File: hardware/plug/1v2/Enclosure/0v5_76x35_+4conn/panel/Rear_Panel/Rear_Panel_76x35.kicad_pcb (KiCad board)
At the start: 2 copper layers, 76 x 35 mm, 6 parts

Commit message: qfix
- #9 documents
- USB and PWR cutout displacement for 0.15 mm
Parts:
- moved REF** 0.15 mm to (56.8, 120.5)
- moved REF** 0.15 mm to (70.6, 120.5)
- moved REF** 0.15 mm to (55.9, 117.8)
- moved REF** 0.15 mm to (71.3, 117.8)
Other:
- outline, holes or cut-outs redrawn

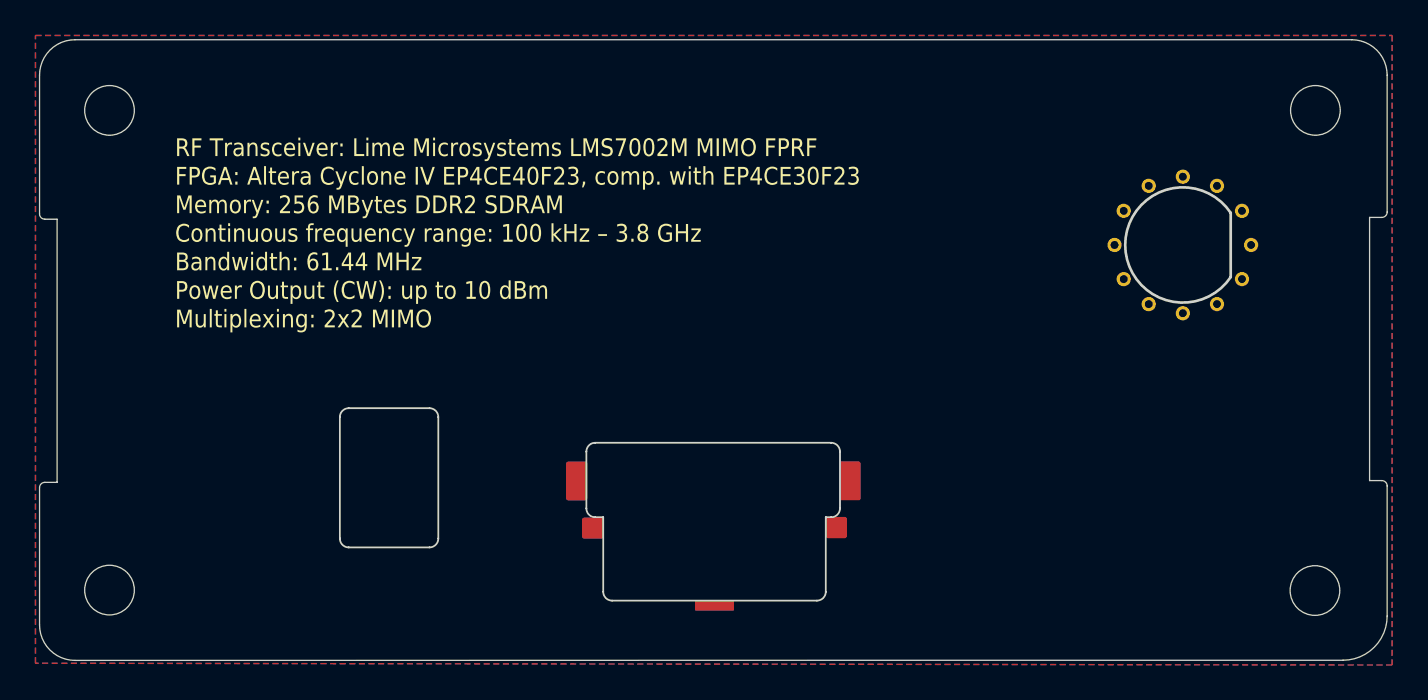
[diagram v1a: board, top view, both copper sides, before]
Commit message: 3rd batch ready for fab house
Gerber output produced
Combined into a panel

Added small holes on backside for "ventilation" #7
Naming is consistent with current LimeSDR boards W, L, H order for TX #2

Text stays on Silkscreen for now #8
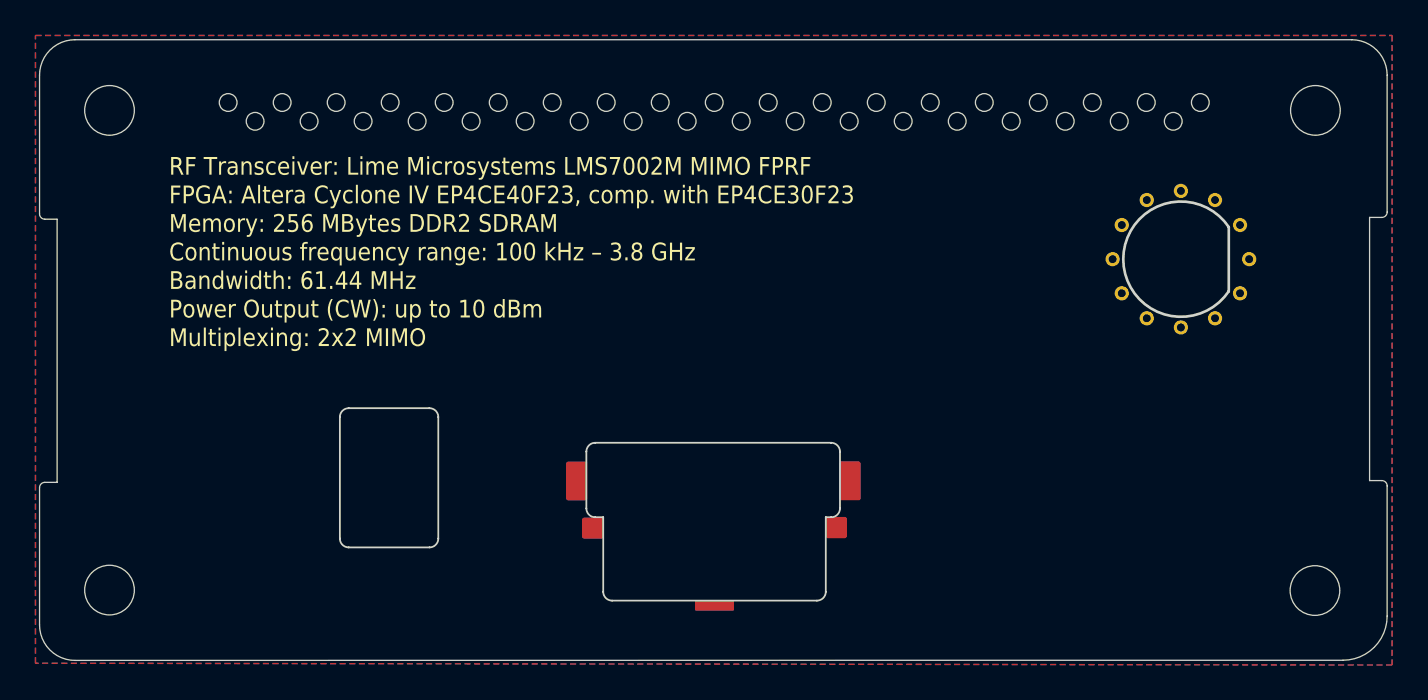
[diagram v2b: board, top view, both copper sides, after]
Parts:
- added REF**: Hole, Ohisja:hole, F.Cu at (43.9, 97.5)
- added REF**: Hole, Ohisja:hole, F.Cu at (68.2, 97.5)
- added REF**: Hole, Ohisja:hole, F.Cu at (71.3, 97.5)
- added REF**: Hole, Ohisja:hole, F.Cu at (65.2, 97.5)
- added REF**: Hole, Ohisja:hole, F.Cu at (56.1, 97.5)
- added REF**: Hole, Ohisja:hole, F.Cu at (89.6, 97.5)
- added REF**: Hole, Ohisja:hole, F.Cu at (80.4, 97.5)
- added REF**: Hole, Ohisja:hole, F.Cu at (83.5, 97.5)
- added REF**: Hole, Ohisja:hole, F.Cu at (86.5, 97.5)
- added REF**: Hole, Ohisja:hole, F.Cu at (77.4, 97.5)
- added REF**: Hole, Ohisja:hole, F.Cu at (91.1, 96.5)
- added REF**: Hole, Ohisja:hole, F.Cu at (46.9, 97.5)
- added REF**: Hole, Ohisja:hole, F.Cu at (88.0, 96.5)
- added REF**: Hole, Ohisja:hole, F.Cu at (85.0, 96.5)
- added REF**: Hole, Ohisja:hole, F.Cu at (81.9, 96.5)
- added REF**: Hole, Ohisja:hole, F.Cu at (78.9, 96.5)
- added REF**: Hole, Ohisja:hole, F.Cu at (75.9, 96.5)
- added REF**: Hole, Ohisja:hole, F.Cu at (72.8, 96.5)
- added REF**: Hole, Ohisja:hole, F.Cu at (69.8, 96.5)
- added REF**: Hole, Ohisja:hole, F.Cu at (66.7, 96.5)
- added REF**: Hole, Ohisja:hole, F.Cu at (63.7, 96.5)
- added REF**: Hole, Ohisja:hole, F.Cu at (60.6, 96.5)
- added REF**: Hole, Ohisja:hole, F.Cu at (37.8, 97.5)
- added REF**: Hole, Ohisja:hole, F.Cu at (57.6, 96.5)
- added REF**: Hole, Ohisja:hole, F.Cu at (54.5, 96.5)
- added REF**: Hole, Ohisja:hole, F.Cu at (51.5, 96.5)
- added REF**: Hole, Ohisja:hole, F.Cu at (48.4, 96.5)
- added REF**: Hole, Ohisja:hole, F.Cu at (45.4, 96.5)
- added REF**: Hole, Ohisja:hole, F.Cu at (42.4, 96.5)
- added REF**: Hole, Ohisja:hole, F.Cu at (39.3, 96.5)
- added REF**: Hole, Ohisja:hole, F.Cu at (53.0, 97.5)
- added REF**: Hole, Ohisja:hole, F.Cu at (40.8, 97.5)
- added REF**: Hole, Ohisja:hole, F.Cu at (50.0, 97.5)
- added REF**: Hole, Ohisja:hole, F.Cu at (74.3, 97.5)
- added REF**: Hole, Ohisja:hole, F.Cu at (59.1, 97.5)
- added REF**: Hole, Ohisja:hole, F.Cu at (62.1, 97.5)
- added REF1: Hole, Ohisja:hole, F.Cu at (36.3, 96.5)
- moved REF** 0.81 mm to (90.0, 105.3)
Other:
- board text added: "20160924"
- board text removed: "20160910"

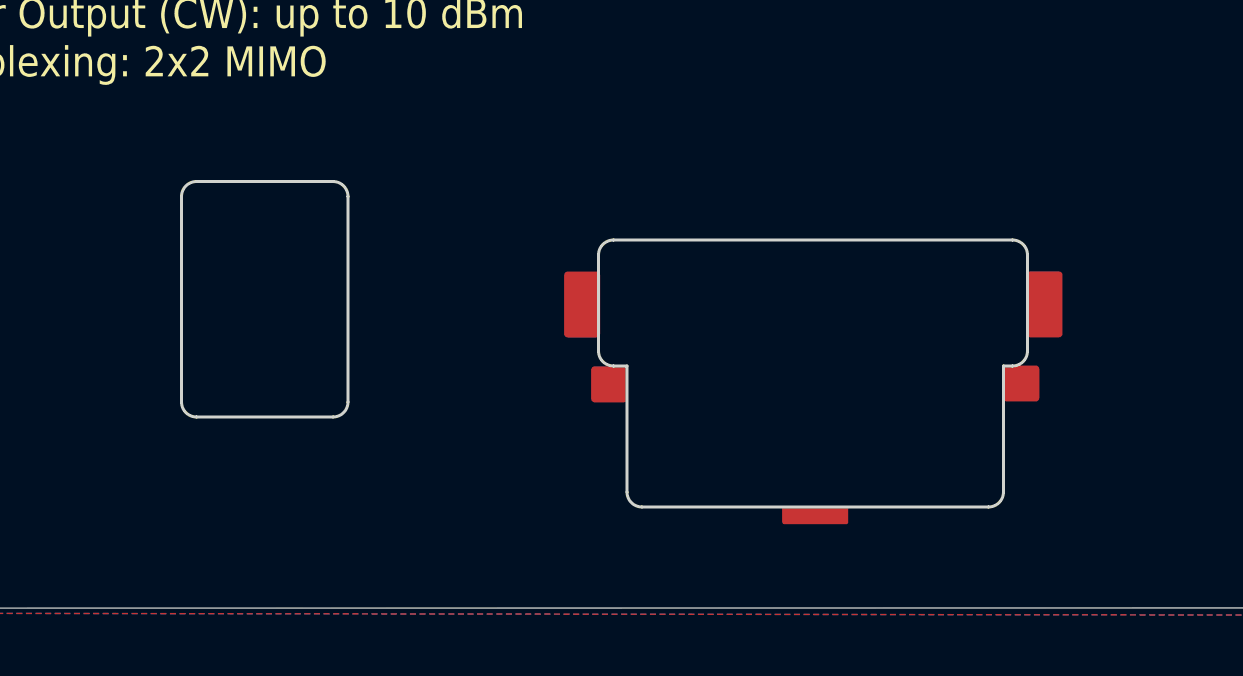
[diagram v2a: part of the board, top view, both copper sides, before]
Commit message: add 3d models in .wrl
used @2ftg .step models and imported them into FreeCAD
added .wrl for Rear panels and hole plugs
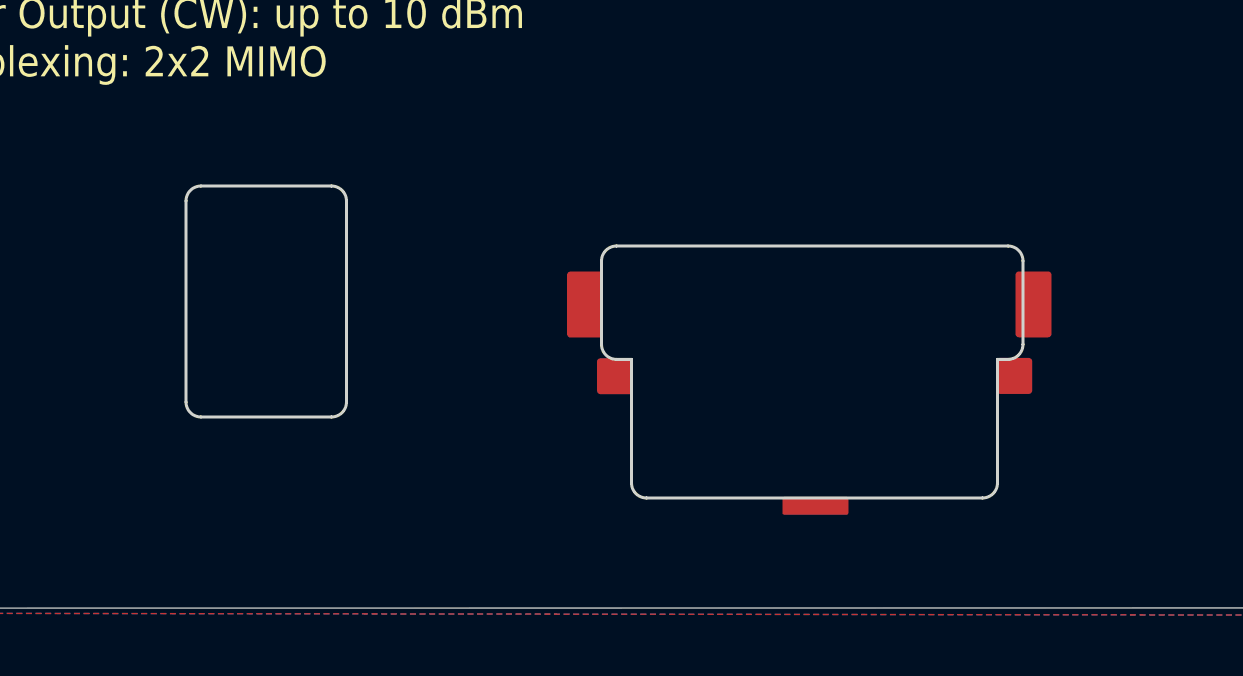
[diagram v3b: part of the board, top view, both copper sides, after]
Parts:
- moved REF** 0.37 mm to (71.0, 117.8)
- moved REF** 0.34 mm to (70.3, 120.2)
- moved REF** 0.33 mm to (57.0, 120.2)
- moved REF** 0.31 mm to (63.7, 124.5)
- moved REF** 0.10 mm to (56.0, 117.8)
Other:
- outline, holes or cut-outs redrawn
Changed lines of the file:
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@@
     (links 16)
     (no_connects 0)
-    (area 25.34 92.7 101.900001 128.200001)
+    (area 25.619999 92.929999 101.630001 127.950001)
     (thickness 1.6)
     (drawings 295)
@@
     (pad_to_mask_clearance 0)
     (aux_axis_origin 24.95 92.3)
-    (grid_origin 24.95 92.3)
+    (grid_origin 56.965227 115.867916)
     (visible_elements 7FFFFFFF)
     (pcbplotparams
@@
   )
   (module Connect:1pin (layer F.Cu)
-    (at 56.82 120.48)
+    (at 57.015227 120.207916)
     (descr "module 1 pin (ou trou mecanique de percage)")
     (tags DEV)
@@
   )
   (module Connect:1pin (layer F.Cu)
-    (at 70.56 120.45)
+    (at 70.325227 120.197916)
     (descr "module 1 pin (ou trou mecanique de percage)")
     (tags DEV)
@@
   )
   (module Connect:1pin (layer F.Cu)
-    (at 63.69 124.84 270)
+    (at 63.695227 124.527916 270)
     (descr "module 1 pin (ou trou mecanique de percage)")
     (tags DEV)
@@
   )
   (module Connect:1pin (layer F.Cu)
-    (at 55.92 117.82 180)
+    (at 56.015227 117.82 180)
     (descr "module 1 pin (ou trou mecanique de percage)")
     (tags DEV)
@@
     (fp_circle (center 0 0) (end 3.83 0) (layer F.Mask) (width 1.35))
     (fp_circle (center 0 0) (end 2.66 0) (layer F.Mask) (width 3))
+    (pad 1 thru_hole circle (at 3.85 0 270) (size 0.8 0.8) (drill 0.45) (layers *.Cu)
+      (net 1 GND))
+    (pad 1 thru_hole circle (at 3.334198 1.925 240) (size 0.8 0.8) (drill 0.45) (layers *.Cu)
+      (net 1 GND))
+    (pad 1 thru_hole circle (at 1.925 3.334198 210) (size 0.8 0.8) (drill 0.45) (layers *.Cu)
+      (net 1 GND))
+    (pad 1 thru_hole circle (at 0 3.85 180) (size 0.8 0.8) (drill 0.45) (layers *.Cu)
+      (net 1 GND))
+    (pad 1 thru_hole circle (at -1.925 3.334198 150) (size 0.8 0.8) (drill 0.45) (layers *.Cu)
+      (net 1 GND))
+    (pad 1 thru_hole circle (at -3.334198 1.925 120) (size 0.8 0.8) (drill 0.45) (layers *.Cu)
+      (net 1 GND))
+    (pad 1 thru_hole circle (at -3.85 0 90) (size 0.8 0.8) (drill 0.45) (layers *.Cu)
+      (net 1 GND))
+    (pad 1 thru_hole circle (at -3.334198 -1.925 60) (size 0.8 0.8) (drill 0.45) (layers *.Cu)
+      (net 1 GND))
+    (pad 1 thru_hole circle (at -1.925 -3.334198 30) (size 0.8 0.8) (drill 0.45) (layers *.Cu)
+      (net 1 GND))
+    (pad 1 thru_hole circle (at 0 -3.85) (size 0.8 0.8) (drill 0.45) (layers *.Cu)
+      (net 1 GND))
+    (pad 1 thru_hole circle (at 1.925 -3.334198 330) (size 0.8 0.8) (drill 0.45) (layers *.Cu)
+      (net 1 GND))
     (pad 1 thru_hole circle (at 3.334198 -1.925 300) (size 0.8 0.8) (drill 0.45) (layers *.Cu)
-      (net 1 GND))
-    (pad 1 thru_hole circle (at 1.925 -3.334198 330) (size 0.8 0.8) (drill 0.45) (layers *.Cu)
-      (net 1 GND))
-    (pad 1 thru_hole circle (at 0 -3.85) (size 0.8 0.8) (drill 0.45) (layers *.Cu)
-      (net 1 GND))
-    (pad 1 thru_hole circle (at -1.925 -3.334198 30) (size 0.8 0.8) (drill 0.45) (layers *.Cu)
-      (net 1 GND))
-    (pad 1 thru_hole circle (at -3.334198 -1.925 60) (size 0.8 0.8) (drill 0.45) (layers *.Cu)
-      (net 1 GND))
-    (pad 1 thru_hole circle (at -3.85 0 90) (size 0.8 0.8) (drill 0.45) (layers *.Cu)
-      (net 1 GND))
-    (pad 1 thru_hole circle (at -3.334198 1.925 120) (size 0.8 0.8) (drill 0.45) (layers *.Cu)
-      (net 1 GND))
-    (pad 1 thru_hole circle (at -1.925 3.334198 150) (size 0.8 0.8) (drill 0.45) (layers *.Cu)
-      (net 1 GND))
-    (pad 1 thru_hole circle (at 0 3.85 180) (size 0.8 0.8) (drill 0.45) (layers *.Cu)
-      (net 1 GND))
-    (pad 1 thru_hole circle (at 1.925 3.334198 210) (size 0.8 0.8) (drill 0.45) (layers *.Cu)
-      (net 1 GND))
-    (pad 1 thru_hole circle (at 3.334198 1.925 240) (size 0.8 0.8) (drill 0.45) (layers *.Cu)
-      (net 1 GND))
-    (pad 1 thru_hole circle (at 3.85 0 270) (size 0.8 0.8) (drill 0.45) (layers *.Cu)
       (net 1 GND))
     (model D:/Dropbox/Projekti/Ohisja/sma.wrl
@@
   )
   (module Connect:1pin (layer F.Cu)
-    (at 71.332739 117.815001 180)
+    (at 70.965227 117.815001 180)
     (descr "module 1 pin (ou trou mecanique de percage)")
     (tags DEV)
@@
     (effects (font (size 1.8 1.8) (thickness 0.3)) (justify mirror))
   )
-  (gr_line (start 69.465227 124.567916) (end 57.915227 124.567916) (layer Edge.Cuts) (width 0.1))
-  (gr_arc (start 69.465227 124.067916) (end 69.965227 124.067916) (angle 90) (layer Edge.Cuts) (width 0.1))
-  (gr_line (start 69.965227 119.867916) (end 69.965227 124.067916) (layer Edge.Cuts) (width 0.1))
-  (gr_line (start 43.065227 121.567916) (end 47.615227 121.567916) (layer Edge.Cuts) (width 0.1))
-  (gr_arc (start 47.615227 121.067916) (end 48.115227 121.067916) (angle 90) (layer Edge.Cuts) (width 0.1))
-  (gr_line (start 48.115227 114.217916) (end 48.115227 121.067916) (layer Edge.Cuts) (width 0.1))
-  (gr_arc (start 47.615227 114.217916) (end 47.615227 113.717916) (angle 90) (layer Edge.Cuts) (width 0.1))
-  (gr_line (start 47.615227 113.717916) (end 43.065227 113.717916) (layer Edge.Cuts) (width 0.1))
-  (gr_arc (start 43.065227 114.217916) (end 42.565227 114.217916) (angle 90) (layer Edge.Cuts) (width 0.1))
-  (gr_line (start 42.565227 114.217916) (end 42.565227 121.067916) (layer Edge.Cuts) (width 0.1))
-  (gr_arc (start 43.065227 121.067916) (end 43.065227 121.567916) (angle 90) (layer Edge.Cuts) (width 0.1))
-  (gr_arc (start 57.915227 124.067916) (end 57.915227 124.567916) (angle 90) (layer Edge.Cuts) (width 0.1))
-  (gr_line (start 57.415227 119.867916) (end 57.415227 124.067916) (layer Edge.Cuts) (width 0.1))
-  (gr_line (start 69.965227 119.867916) (end 70.265227 119.867916) (layer Edge.Cuts) (width 0.1))
-  (gr_line (start 57.415227 119.867916) (end 56.965227 119.867916) (layer Edge.Cuts) (width 0.1))
-  (gr_arc (start 70.265227 119.367916) (end 70.765227 119.367916) (angle 90) (layer Edge.Cuts) (width 0.1))
-  (gr_line (start 70.765227 116.167916) (end 70.765227 119.367916) (layer Edge.Cuts) (width 0.1))
-  (gr_arc (start 56.965227 119.367916) (end 56.965227 119.867916) (angle 90) (layer Edge.Cuts) (width 0.1))
-  (gr_line (start 56.465227 116.167916) (end 56.465227 119.367916) (layer Edge.Cuts) (width 0.1))
-  (gr_arc (start 56.965227 116.167916) (end 56.465227 116.167916) (angle 90) (layer Edge.Cuts) (width 0.1))
-  (gr_line (start 70.265227 115.667916) (end 56.965227 115.667916) (layer Edge.Cuts) (width 0.1))
-  (gr_arc (start 70.265227 116.167916) (end 70.265227 115.667916) (angle 90) (layer Edge.Cuts) (width 0.1))
+  (gr_line (start 69.265227 124.267916) (end 58.065227 124.267916) (layer Edge.Cuts) (width 0.1))
+  (gr_arc (start 69.265227 123.767916) (end 69.765227 123.767916) (angle 90) (layer Edge.Cuts) (width 0.1))
+  (gr_line (start 69.765227 119.647916) (end 69.765227 123.767916) (layer Edge.Cuts) (width 0.1))
+  (gr_line (start 43.215227 121.567916) (end 47.565227 121.567916) (layer Edge.Cuts) (width 0.1))
+  (gr_arc (start 47.565227 121.067916) (end 48.065227 121.067916) (angle 90) (layer Edge.Cuts) (width 0.1))
+  (gr_line (start 48.065227 114.367916) (end 48.065227 121.067916) (layer Edge.Cuts) (width 0.1))
+  (gr_arc (start 47.565227 114.367916) (end 47.565227 113.867916) (angle 90) (layer Edge.Cuts) (width 0.1))
+  (gr_line (start 47.565227 113.867916) (end 43.215227 113.867916) (layer Edge.Cuts) (width 0.1))
+  (gr_arc (start 43.215227 114.367916) (end 42.715227 114.367916) (angle 90) (layer Edge.Cuts) (width 0.1))
+  (gr_line (start 42.715227 114.367916) (end 42.715227 121.067916) (layer Edge.Cuts) (width 0.1))
+  (gr_arc (start 43.215227 121.067916) (end 43.215227 121.567916) (angle 90) (layer Edge.Cuts) (width 0.1))
+  (gr_arc (start 58.065227 123.767916) (end 58.065227 124.267916) (angle 90) (layer Edge.Cuts) (width 0.1))
+  (gr_line (start 57.565227 119.647916) (end 57.565227 123.767916) (layer Edge.Cuts) (width 0.1))
+  (gr_line (start 69.765227 119.647916) (end 70.115227 119.647916) (layer Edge.Cuts) (width 0.1))
+  (gr_line (start 57.565227 119.647916) (end 57.065227 119.647916) (layer Edge.Cuts) (width 0.1))
+  (gr_arc (start 70.115227 119.147916) (end 70.615227 119.147916) (angle 90) (layer Edge.Cuts) (width 0.1))
+  (gr_line (start 70.615227 116.367916) (end 70.615227 119.147916) (layer Edge.Cuts) (width 0.1))
+  (gr_arc (start 57.065227 119.147916) (end 57.065227 119.647916) (angle 90) (layer Edge.Cuts) (width 0.1))
+  (gr_line (start 56.565227 116.367916) (end 56.565227 119.147916) (layer Edge.Cuts) (width 0.1))
+  (gr_arc (start 57.065227 116.367916) (end 56.565227 116.367916) (angle 90) (layer Edge.Cuts) (width 0.1))
+  (gr_line (start 70.115227 115.867916) (end 57.065227 115.867916) (layer Edge.Cuts) (width 0.1))
+  (gr_arc (start 70.115227 116.367916) (end 70.115227 115.867916) (angle 90) (layer Edge.Cuts) (width 0.1))
   (gr_line (start 37.384773 99.597916) (end 36.984773 99.997917) (layer Dwgs.User) (width 0.2))
   (gr_line (start 36.984773 99.597916) (end 37.384774 99.997915) (layer Dwgs.User) (width 0.2))
